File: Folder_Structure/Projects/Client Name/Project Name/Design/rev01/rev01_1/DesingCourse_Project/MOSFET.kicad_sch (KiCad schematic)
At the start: 30 parts, among them J6 7461084, J7 7461084, J8 7461084, Q1 HSBA15810C, Q2 HSBA15810C, Q3 HSBA15810C, Q4 HSBA15810C, Q5 HSBA15810C, Q6 HSBA15810C

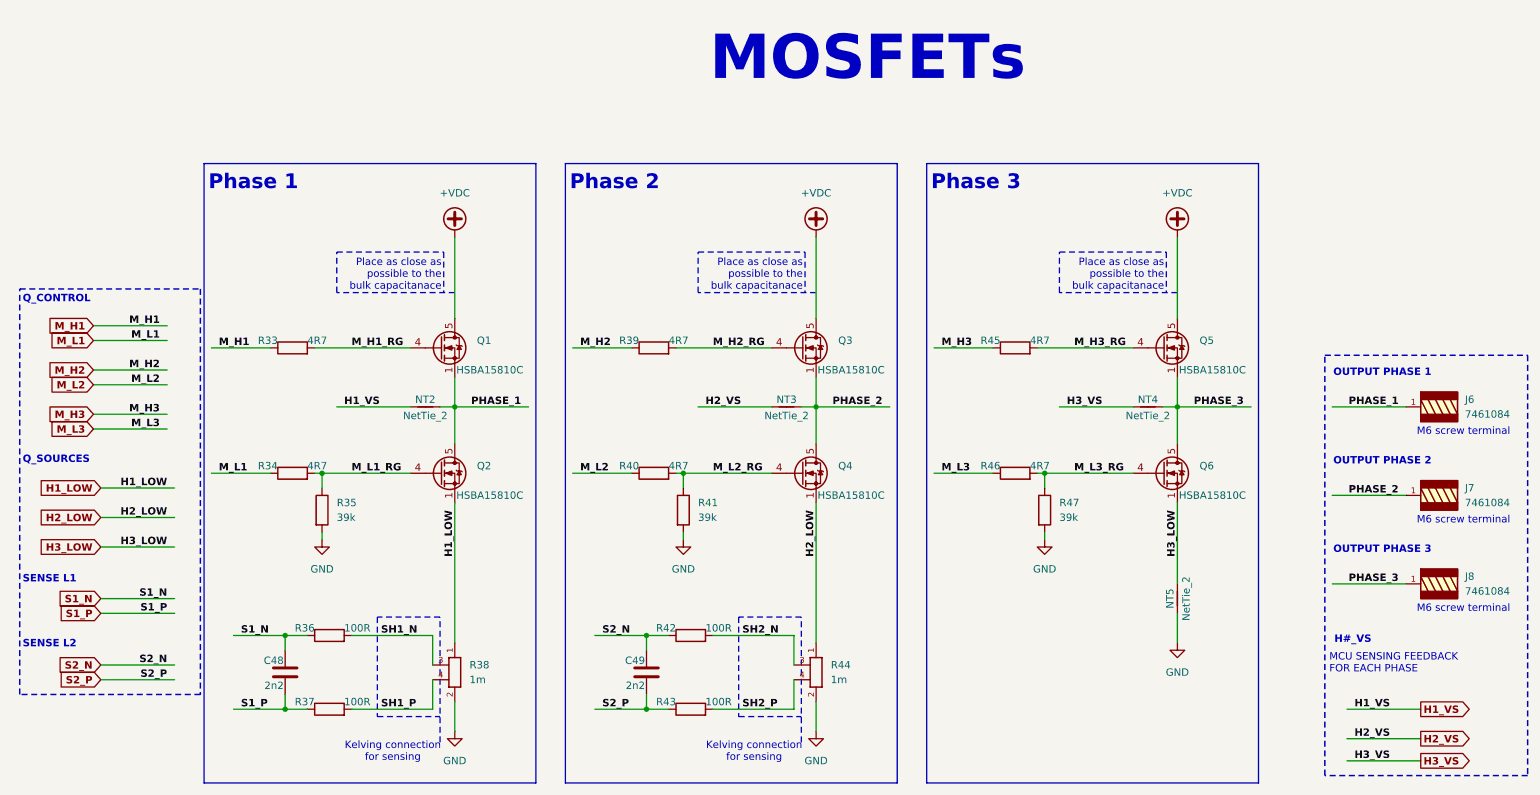
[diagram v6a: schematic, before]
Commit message: Update 16
Initial component placement done
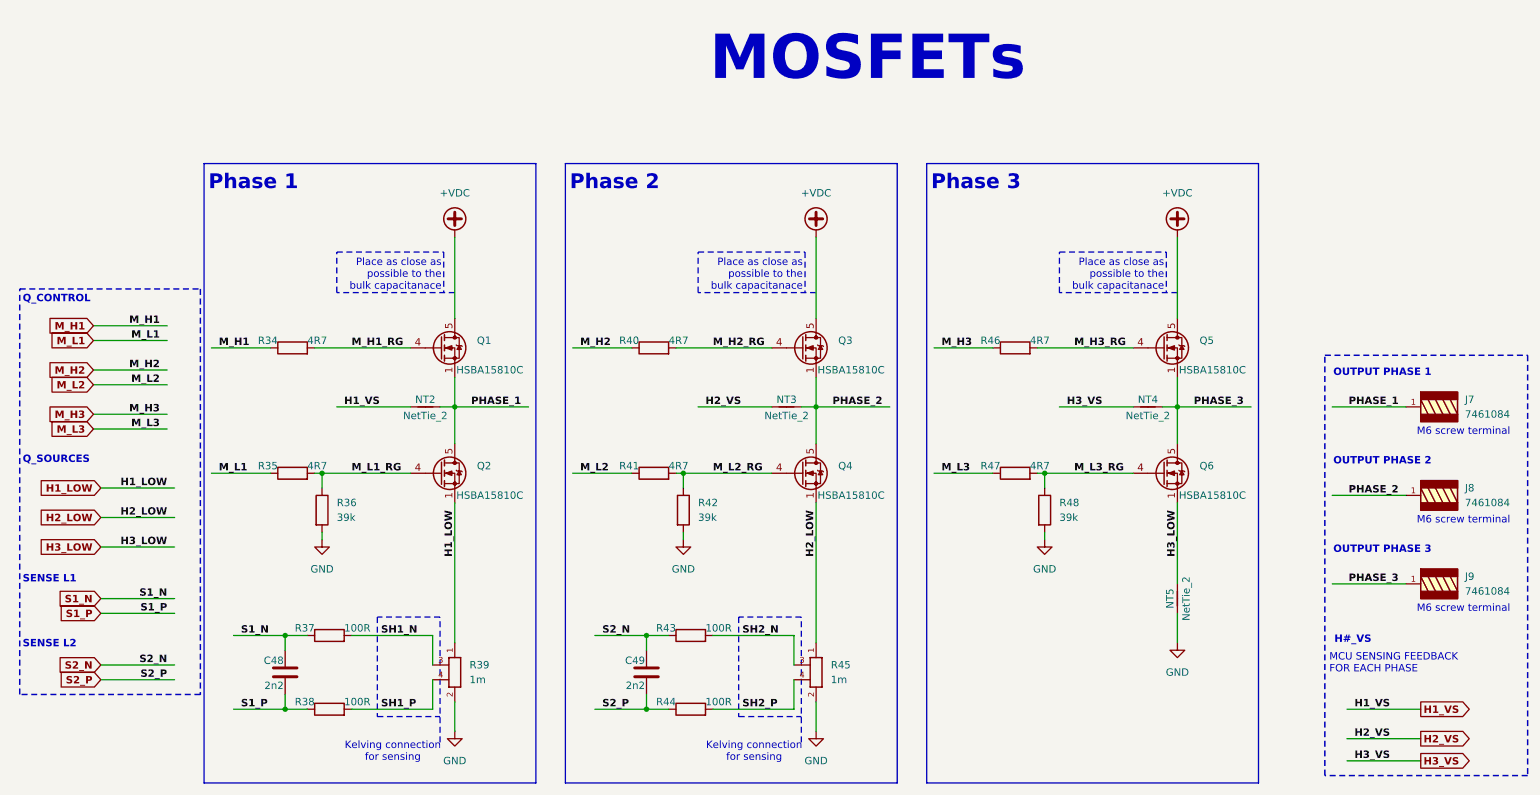
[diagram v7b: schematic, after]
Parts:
- Q1, Q2, Q3, Q4, Q5, Q6: footprint Package_SO:PowerPAK_SO-8_Single -> Package_SO:HSBA15810C; Package (none) -> 8pin-PRPAK5x6
- renumbered J6 to J7, J7 to J8, J8 to J9, R33 to R34, R34 to R35, R35 to R36, R36 to R37, R37 to R38, R38 to R39, R39 to R40, R40 to R41, R41 to R42, R42 to R43, R43 to R44, R44 to R45, R45 to R46, R46 to R47, R47 to R48
